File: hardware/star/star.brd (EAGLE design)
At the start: 116.5 x 163.8 mm, 165 parts, among them IC1 MAX481CSA, IC2 LD117AS12TR, IC22 LD117AS12TR, IC3 74HCT08D, IC4 7404D, IC5 LM317MABDT, IC6 LM317MABDT, IC7 LM317MABDT, IC8 MAX481CSA, IC9 LD117AS12TR, K1 T90-12VDC-TL-A, K2 T90-12VDC-TL-A, P1 B3B-PH-K, Q1 35A/25V/8.5mΩ, Q2 35A/25V/8.5mΩ, Q3 35A/25V/8.5mΩ, Q4 35A/25V/8.5mΩ, T1 T_PNP_MMBT5401_CHANGJ_SOT23-B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, T2 T_PNP_MMBT5401_CHANGJ_SOT23-B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, T3 T_PNP_MMBT5401_CHANGJ_SOT23-B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, T4 T_PNP_MMBT5401_CHANGJ_SOT23-B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, U1 TCLT1600, X1 MKDSN1,5/2-5,08, X3 MKDSN1,5/5-5,08

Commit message: update
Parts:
- added R6: R_0R_1206, JLC PCB Basic Parts_loc:R1206
- FIRE: device con-phoenix-508:MKDSN1,5/8-5,08 -> con-phoenix-508-jm:MKDSN1,5/8-5,08
- POWER_IN: device con-phoenix-508:MKDSN1,5/4-5,08 -> con-phoenix-508-jm:MKDSN1,5/4-5,08
- R132: value 12k -> 1k
- X1: device con-phoenix-508:MKDSN1,5/2-5,08 -> con-phoenix-508-jm:MKDSN1,5/2-5,08
- X3: device con-phoenix-508:MKDSN1,5/5-5,08 -> con-phoenix-508-jm:MKDSN1,5/5-5,08
- moved C22 3.17 mm to (103.5, 94.6)
- moved C23 3.17 mm to (97.8, 92.7)
- moved D9 3.17 mm to (87.0, 94.6)
- moved R38 3.17 mm to (100.3, 92.7)
- moved R39 3.17 mm to (100.3, 96.5)
- moved R40 3.17 mm to (97.8, 96.5)
- moved R41 3.17 mm to (89.5, 94.6)
- moved R42 3.17 mm to (84.5, 94.6)
- moved R43 3.17 mm to (81.9, 94.6)
- moved T4 3.17 mm to (93.3, 94.6)
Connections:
- net GND: now also R6.1
- net GND2: now also R6.2
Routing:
- net GND: track 441.0 -> 0.00 mm, vias 8 -> 0
- net +12V: track 398.5 -> 0.00 mm, vias 6 -> 0
- net +5V: track 380.2 -> 0.00 mm, vias 5 -> 0
- net +3V3: track 368.7 -> 0.00 mm, vias 9 -> 0
- net 60VDC: track 218.8 -> 0.00 mm
- net 19: track 184.6 -> 0.00 mm
- net LOCAL_EN: track 175.0 -> 0.00 mm, vias 3 -> 0
- net GND2: track 172.8 -> 0.00 mm
- net 18: track 166.9 -> 0.00 mm
- net EN_STATUS: track 159.4 -> 0.00 mm, vias 2 -> 0
- net 17: track 143.6 -> 0.00 mm, vias 1 -> 0
- net 16: track 141.6 -> 0.00 mm, vias 2 -> 0
- net +6V: track 136.4 -> 0.00 mm
- net 21/SDA: track 130.2 -> 0.00 mm
- net 22/SCL: track 120.1 -> 0.00 mm
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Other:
- board text added: "12v"
- board text added: "3.3v"
- board text added: "5v"
- board text added: "60v"
- board text added: "6v"
- board text added: "En Poof Ign Fuel Blow Gnd"

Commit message: Added buckboost
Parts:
- removed C26, C30: 1uf, rcl:C0805
- removed C27, C31: 10uf, rcl:C0603
- removed C29: (no value), rcl:EB25D
- removed D10, D11: MBR20200CT, MBR20200CT:TO254P1050X476X2020-3
- removed IC5, IC6, IC7: LM317MABDT, v-reg:DPACK
- removed R50, R53, R58: R_240R_0603, JLC PCB Basic Parts_loc:R0603
- removed R51, R54, R59: R_750R_0603, JLC PCB Basic Parts_loc:R0603
- removed R52, R6: R_0R_1206, JLC PCB Basic Parts_loc:R1206
- removed R57: S14K420, varistor:S14K420
- added K5, K6: AQG22110, relay:AQG
- added U$2: ZK-SJVA-4X, Nova:ZK-SJVA-4X
- added X2: MKDSN1,5/2-5,08, con-phoenix-508-jm:MKDSN1,5/2-5,08
- C25: value 10uf -> 1uf; device rcl:C0603 -> rcl:C0805
- R55, R56: value S14K420 -> S10K40; device varistor:S14K420 -> varistor:S10K40
- R60, R61: value R_56K_0805 -> R_1K_0603; device JLC PCB Basic Parts_loc:R0805 -> JLC PCB Basic Parts_loc:R0603
- R62: value R_56K_0805 -> R_7.5K_0603; device JLC PCB Basic Parts_loc:R0805 -> JLC PCB Basic Parts_loc:R0603
- R63: value R_2.2K_0603 -> R_1K_0603
- moved D12 52.6 mm to (58.4, 106.0)
- moved D13 52.6 mm to (58.4, 96.5)
- moved D14 52.6 mm to (58.4, 86.4)
- moved D15 52.6 mm to (58.4, 76.2)
- moved D16 52.6 mm to (61.6, 74.3)
- moved R61 52.6 mm to (55.2, 97.8)
- moved R63 52.6 mm to (55.2, 78.1)
- moved D17 52.6 mm to (61.6, 84.5)
- moved D18 52.6 mm to (61.6, 94.6)
- moved D19 52.6 mm to (61.6, 104.1)
- moved Q1 52.6 mm to (67.9, 107.3)
- moved Q2 52.6 mm to (67.9, 97.8)
- moved Q3 52.6 mm to (67.9, 87.6)
- moved Q4 52.6 mm to (67.9, 77.5)
- moved R60 52.6 mm to (55.2, 107.3)
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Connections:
- removed net +6V: D15.C, D16.A, FIRE.1, IC5.4, IC6.4, IC7.4, R50.2, R53.2, R58.2
- removed net 60VDC: C29.+, D10.2, D12.C, D13.C, D14.C, D17.A, D18.A, D19.A, FIRE.3, FIRE.5, FIRE.7
- removed net N$53: IC7.1, R58.1, R59.2
- new net +14V: C25.1, D14.C, D17.A, FIRE.3, U$2.OUT+
- new net +5V/2: D15.C, D16.A, FIRE.1, X2.2
- net +12V: now also U$2.IN+; no longer C25.1, C26.1, C27.1, C30.1, C31.1, IC5.3, IC6.3, IC7.3
- net +5V: now also D12.C, D13.C, D18.A, D19.A, K5.+, K6.+
- net 120_LINE: now also K5.O1, K6.O1; no longer D10.1, D10.3, R57.1
- net 120_NEUTRAL: now also FIRE.6, FIRE.8; no longer D11.2, R57.2
- net GND: now also C24.2, C25.2, Q3.3, U$2.IN-, U$2.OUT-, X2.1; no longer R52.1, R6.1
- net GND2: no longer C29.-, D11.1, D11.3, Q3.3, R6.2
- net GND3: no longer C24.2, C25.2, C26.2, C27.2, C30.2, C31.2, R51.1, R52.2, R54.1, R59.1
- net N$47: now also K5.-; no longer FIRE.6
- net N$48: now also FIRE.7, K6.O2; no longer IC6.1, R53.1, R54.2
- net N$49: now also K6.-; no longer FIRE.8
- net N$50: now also FIRE.5, K5.O2; no longer IC5.1, R50.1, R51.2
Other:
- board size 116.5 x 163.8 mm -> 139.4 x 187.9 mm
- board text added: "GND 5v/2"
- board text removed: "60v"
- board text removed: "6v"

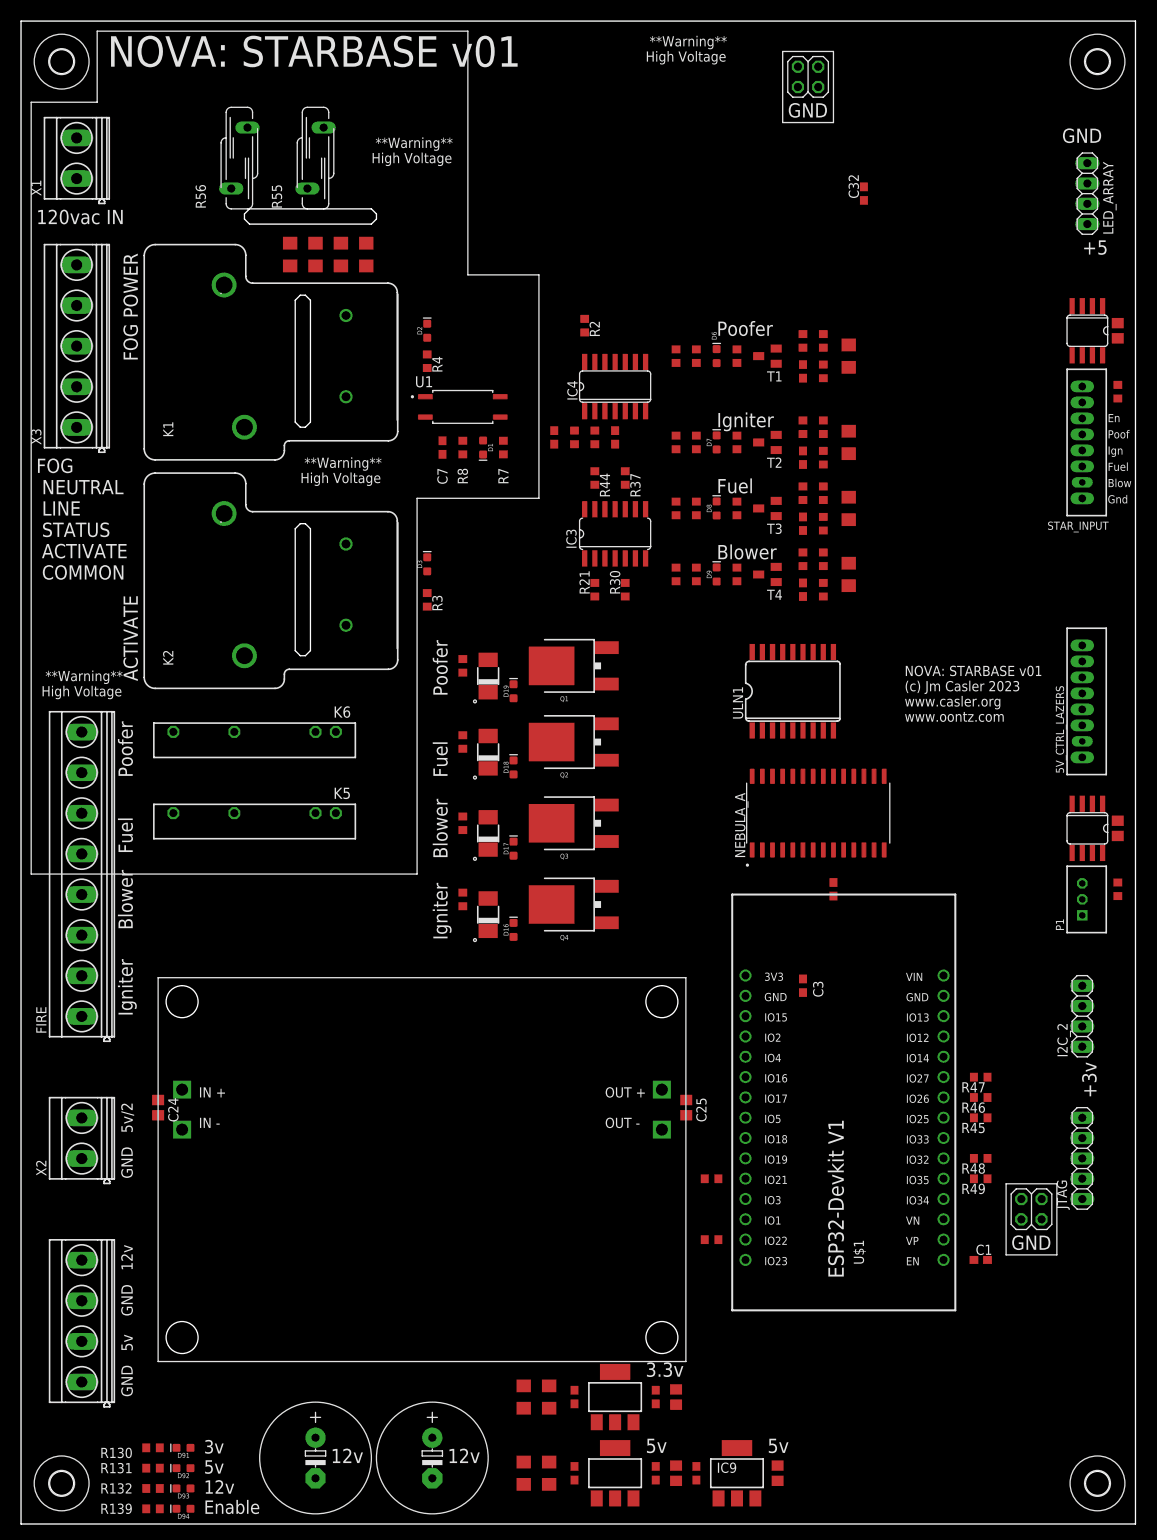
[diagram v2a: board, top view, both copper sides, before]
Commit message: Add TVS diodes
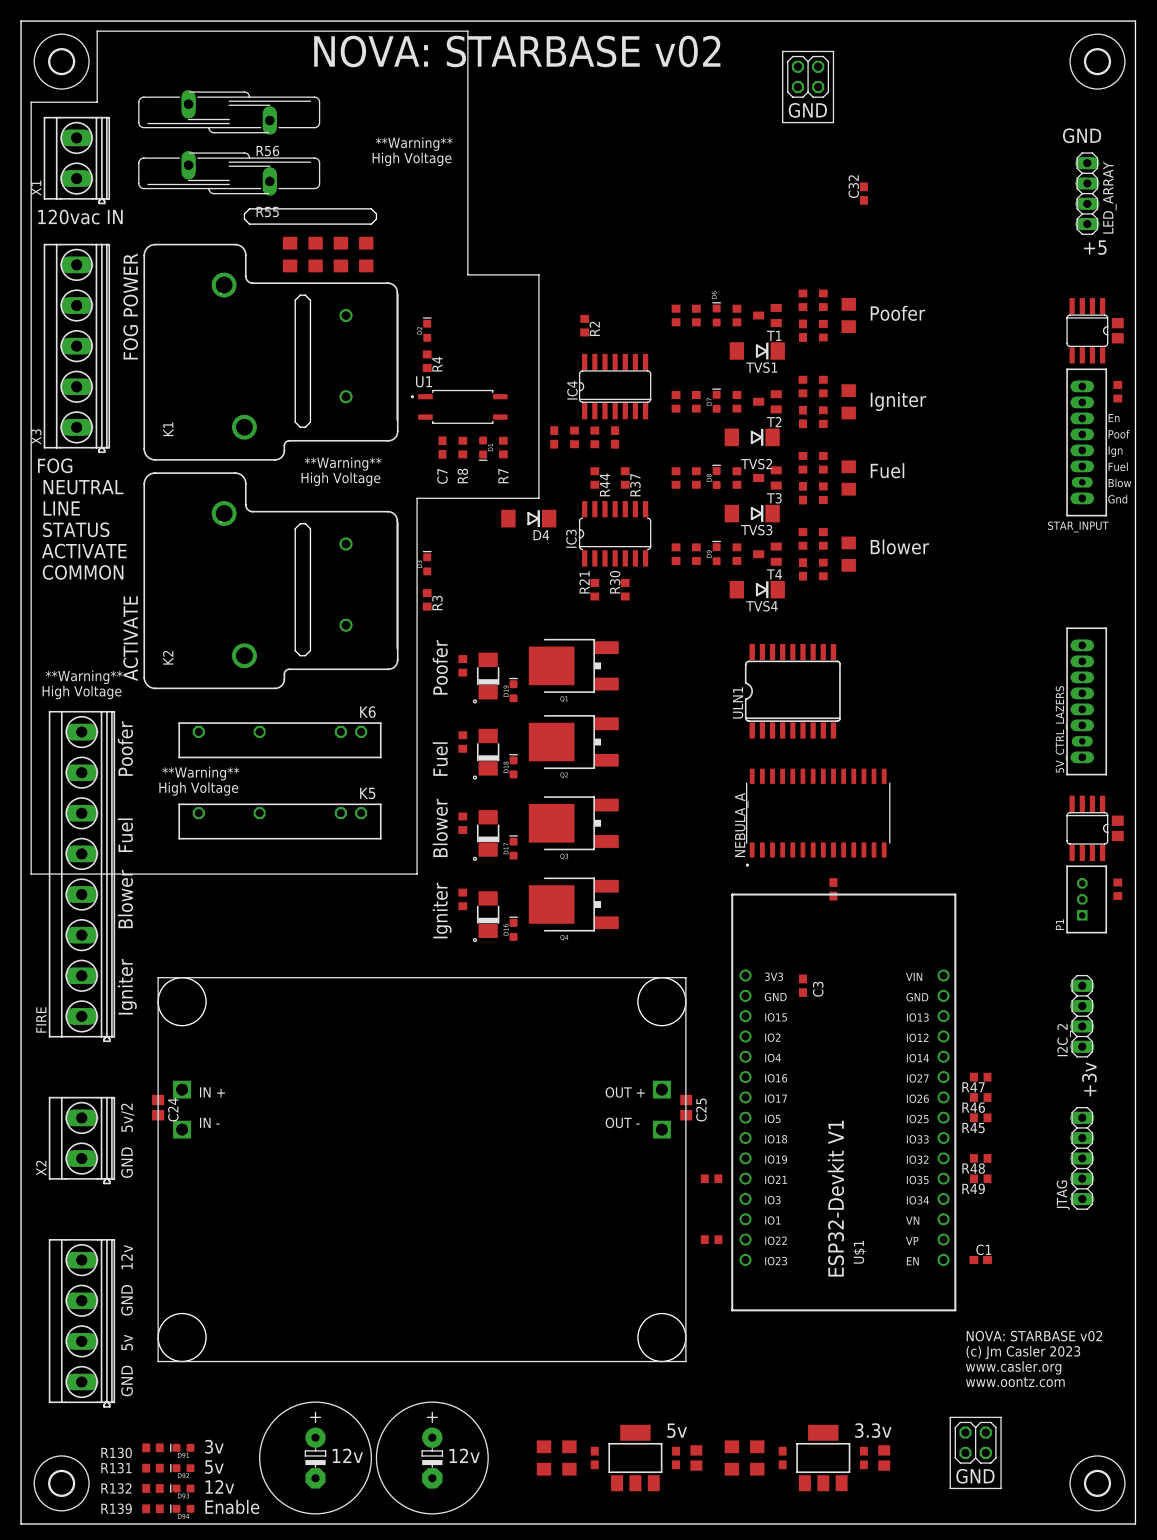
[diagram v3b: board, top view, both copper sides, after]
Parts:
- removed C34: 1uf, rcl:C0805
- removed C37: 10uf, rcl:C0603
- removed IC9: LD117AS12TR, v-reg:SOT223
- added D4, TVS1, TVS2, TVS3, TVS4: (no value), diode:DO214AA
- R14, R23, R32, R39: value R_2K_0603 -> R_10K_0603
- R22, R31, R38, R9: value R_7.5K_0603 -> R_330R_0603
- R55, R56: value S10K40 -> S20K20; device varistor:S10K40 -> varistor:S20K20
- moved JP2 30.0 mm to (119.4, 10.2)
- moved C12 27.1 mm to (88.9, 8.26)
- moved C11 27.1 mm to (92.1, 8.26)
- moved C35 27.1 mm to (105.4, 8.26)
- moved C36 27.1 mm to (95.2, 8.26)
- moved C6 27.1 mm to (108.0, 8.26)
- moved IC22 27.1 mm to (100.3, 8.26)
- moved R55 11.0 mm to (26.0, 168.9), turned to 90 degrees
- moved R56 5.85 mm to (26.0, 176.5), turned to 90 degrees
- moved C18 5.08 mm to (103.5, 140.3)
- moved C19 5.08 mm to (97.8, 138.4)
- moved D7 5.08 mm to (87.0, 140.3)
- moved R22 5.08 mm to (100.3, 138.4)
- moved R23 5.08 mm to (100.3, 142.2)
- moved R24 5.08 mm to (97.8, 142.2)
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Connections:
- net +12V: no longer C34.1, IC9.3, R14.2, R23.2, R32.2, R39.2
- net +5V: no longer C37.1, IC9.4
- net GND: now also D4.A, R14.1, R23.1, R32.1, R39.1, TVS1.A, TVS2.A, TVS3.A, TVS4.A; no longer C34.2, C37.2, IC9.1
- net N$17: now also R14.2, TVS1.C; no longer R14.1
- net N$23: now also D4.C
- net N$25: now also R23.2, TVS4.C; no longer R23.1
- net N$31: now also R32.2, TVS2.C; no longer R32.1
- net N$37: now also R39.2, TVS3.C; no longer R39.1
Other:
- board text added: "NOVA: STARBASE v02"
- board text added: "NOVA: STARBASE v02 (c) Jm Casler 2023 www.casler.org www.oontz.com"
- board text removed: "NOVA: STARBASE v01"
- board text removed: "NOVA: STARBASE v01 (c) Jm Casler 2023 www.casler.org www.oontz.com"

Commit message: I think it's good?
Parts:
- removed FIRE: MKDSN1,5/8-5,08, con-phoenix-508-jm:MKDSN1,5/8-5,08
- removed TVS1, TVS2, TVS3, TVS4: (no value), diode:DO214AA
- added D10, D11, D139, D20, D21, D5: SMBJ8.0CA, SMBJ8.0CA:DIOM4336X265N
- added D22, D23, D24, D25, D26, D27, D28, D29, D30, D31: D_B5819W-SL_CHANGJ_SOD123, JLC PCB Basic Parts_loc:SOD123
- added FIRE_OUT: MKDSN1,5/8-5,08, con-phoenix-508-jm:MKDSN1,5/8-5,08
- added K3: T90-12VDC-TL-A, relay:JT1A-PCB
- added OVERRIDE_EN: B3B-PH-K, con-jst-ph:B3B-PH-K
- added OVERRIDE_EN2: (no value), pinhead:1X03
- added R50: R_1K_0603, JLC PCB Basic Parts_loc:R0603
- added R6: R_100K_0603, JLC PCB Basic Parts_loc:R0603
- D4: value (none) -> SMBJ8.0CA; device diode:DO214AA -> SMBJ8.0CA:DIOM4336X265N
- LED_ARRAY: value (none) -> B4B-PH-K; device pinhead:1X04 -> con-jst-ph:B4B-PH-K
- moved D4 74.6 mm to (123.8, 169.5), turned to 0 degrees
- moved D3 40.7 mm to (53.3, 160.7), turned to 180 degrees
- moved C32 31.8 mm to (137.2, 166.4)
- moved D1 29.5 mm to (53.3, 163.8), turned to 180 degrees
- moved JP1 27.7 mm to (71.1, 176.5)
- moved R4 23.6 mm to (53.3, 168.9), turned to 180 degrees
- moved D2 17.3 mm to (53.3, 166.4), turned to 180 degrees
- moved K5 12.8 mm to (34.3, 101.6)
- moved K6 8.47 mm to (34.3, 107.3)
- moved K2 5.72 mm to (40.6, 123.2)
- moved R10 5.72 mm to (43.2, 164.5)
- moved R11 5.72 mm to (40.0, 164.5)
- moved R12 5.72 mm to (36.8, 164.5)
- moved R13 5.72 mm to (33.7, 164.5)
- moved R55 5.72 mm to (26.0, 174.6)
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- renumbered P1 to DMX_OUT, X1 to 12VAC_IN, X2 to 5V/2_IN, X3 to FOG_IN
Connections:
- new net N$53: FIRE_OUT.1, K3.C
- new net N$58: OVERRIDE_EN.1, OVERRIDE_EN2.1, R50.2
- net +14V: now also FIRE_OUT.3; no longer FIRE.3
- net +3V3: now also D22.C, D24.C, D26.C, D28.C, D30.C, R50.1
- net +5V: now also D15.C, D16.A, K3.1
- net +5V/2: now also K3.NO; no longer D15.C, D16.A, FIRE.1
- net 120_NEUTRAL: now also FIRE_OUT.6, FIRE_OUT.8; no longer FIRE.6, FIRE.8
- net 18: now also D21.2
- net 19: now also D4.2
- net BOOMER_BLOWER: now also D10.2
- net BOOMER_FUEL: now also D5.2
- net BOOMER_IGNITER: now also D11.2
- net GND: now also D10.1, D11.1, D139.1, D20.1, D21.1, D23.A, D25.A, D27.A, D29.A, D31.A, D4.1, D5.1, OVERRIDE_EN.3, OVERRIDE_EN2.3, Q4.3, R6.1; no longer 5V/2_IN.1, D4.A, TVS1.A, TVS2.A, TVS3.A, TVS4.A
- net GND3: now also 5V/2_IN.1, FIRE_OUT.2; no longer Q4.3
- net N$17: now also D22.A, D23.C; no longer TVS1.C
- net N$22: now also OVERRIDE_EN.2, OVERRIDE_EN2.2
- net N$23: now also D30.A, D31.C, R6.2; no longer D4.C
- net N$25: now also D28.A, D29.C; no longer TVS4.C
- net N$31: now also D24.A, D25.C; no longer TVS2.C
- net N$37: now also D26.A, D27.C; no longer TVS3.C
- net N$48: now also FIRE_OUT.7; no longer FIRE.7
- net N$50: now also FIRE_OUT.5; no longer FIRE.5
- net N$51: now also FIRE_OUT.4; no longer FIRE.4
- net N$52: now also K3.2; no longer FIRE.2
- net POOFER: now also D139.2
- net STAR_ENABLE: now also D20.2
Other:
- outline, holes or cut-outs redrawn
- board text added: "FUEL"
- board text added: "Fog Power Fog Ready Fog Active"
- board text added: "IGNITER"
- board text added: "Nova: StarBase"
- board text added: "POOFER"
- board text removed: "NOVA: STARBASE v02"
